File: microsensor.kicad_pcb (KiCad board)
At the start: 2 copper layers, 35 x 47.8 mm, 24 parts, among them J1 ARM SWD, SW1 Control, U1 BMD-360-A-R, U2 RV-3028-C7, U3 HDC2080

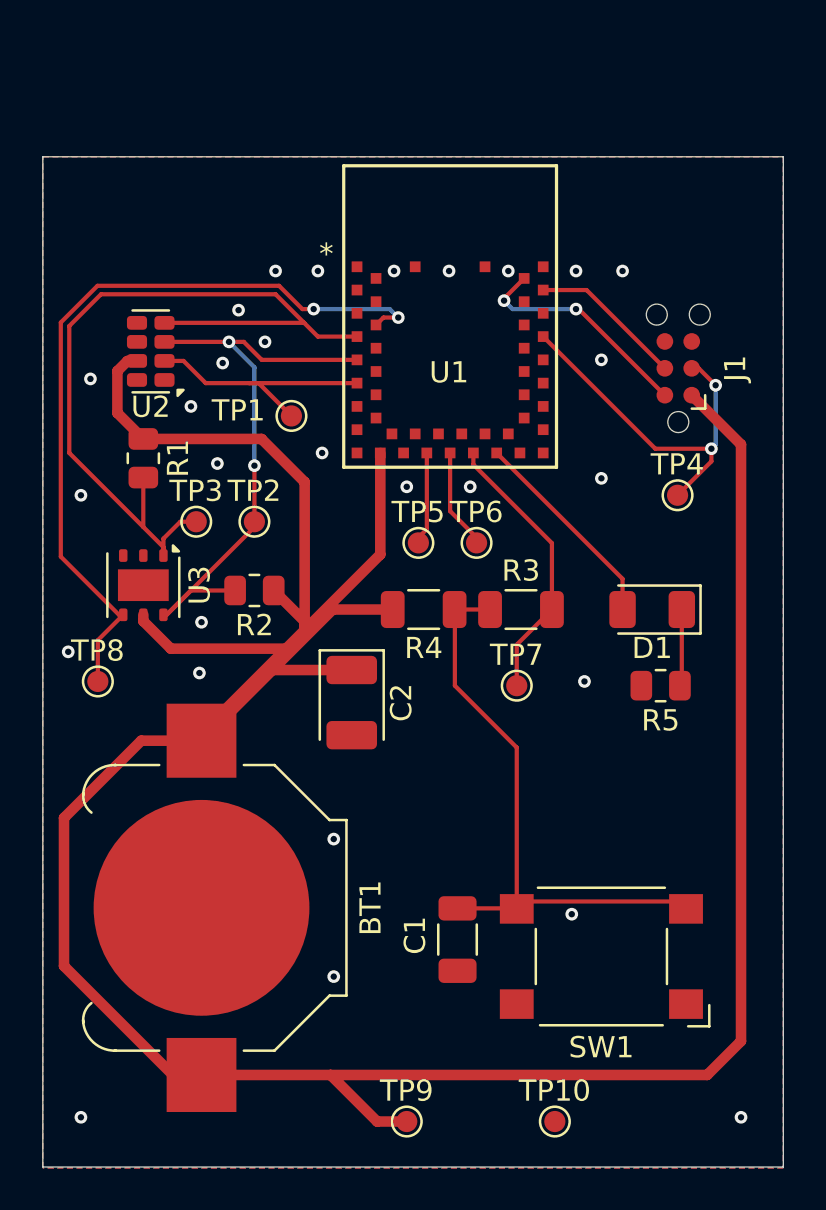
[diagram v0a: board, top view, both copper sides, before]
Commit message: Shrink to 45x35 Unify R sizes to 0805 Rearrange Add dimensions (User layer)
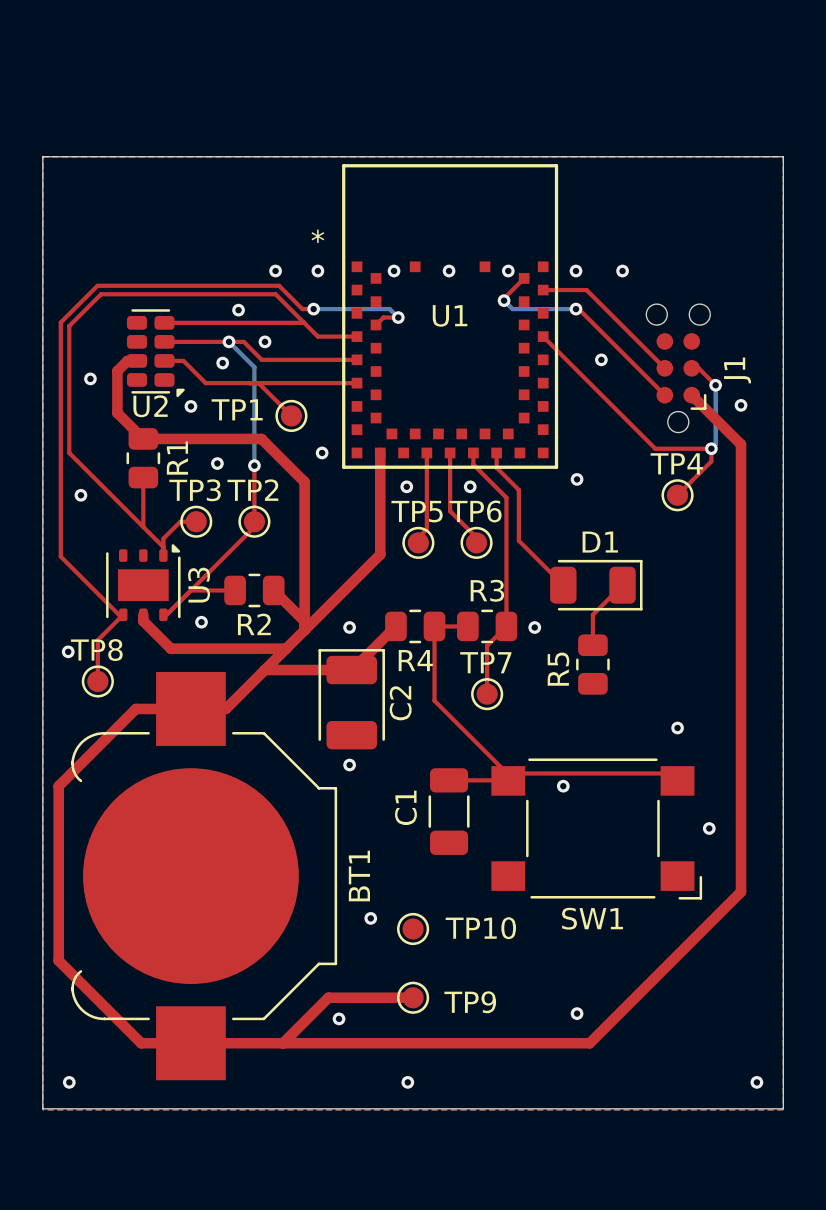
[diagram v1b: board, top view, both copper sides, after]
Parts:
- R3, R4: footprint Resistor_SMD:R_1206_3216Metric -> Resistor_SMD:R_0805_2012Metric
- moved TP10 11.3 mm to (47.5, 66.5)
- moved C1 6.06 mm to (49.2, 61.0)
- moved SW1 6.06 mm to (56.0, 61.8)
- moved TP9 5.86 mm to (47.5, 69.8)
- moved R5 3.35 mm to (56.0, 54.0), turned to -90 degrees
- moved D1 3.03 mm to (56.0, 50.2)
- moved R3 1.79 mm to (51.0, 52.2)
- moved BT1 1.58 mm to (37.0, 64.0)
- moved TP7 1.46 mm to (51.0, 55.4)
- moved R4 0.89 mm to (47.6, 52.2)
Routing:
- net +3V3: track 151.7 -> 138.9 mm
- net Net-(C1-Pad1): track 28.7 -> 22.0 mm
- net Net-(D1-A): track 9.86 -> 7.55 mm
- net SWPUSH: track 13.2 -> 12.4 mm
- net GND: vias 28 -> 34
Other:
- board size 35 x 47.8 mm -> 35 x 45 mm

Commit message: Ver 0.1 finalized and ordered
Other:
- board text added: "BLEsensor v0.1"
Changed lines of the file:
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@@
 				(type "Bottom Silk Screen")
 			)
-			(copper_finish "None")
+			(copper_finish "ENIG")
 			(dielectric_constraints no)
 		)
@@
 			(disableapertmacros no)
 			(usegerberextensions no)
-			(usegerberattributes yes)
+			(usegerberattributes no)
 			(usegerberadvancedattributes yes)
 			(creategerberjobfile yes)
@@
 			(outputformat 1)
 			(mirror no)
-			(drillshape 1)
+			(drillshape 0)
 			(scaleselection 1)
-			(outputdirectory "")
+			(outputdirectory "./CAM")
 		)
 	)
@@
 		(tags "test point SMD pad")
 		(property "Reference" "TP3"
-			(at 0 -1.448 0)
+			(at -0.063609 -1.468763 0)
 			(layer "F.SilkS")
 			(effects
@@
 		(tags "test point SMD pad")
 		(property "Reference" "TP5"
-			(at 0 -1.448 0)
+			(at -0.430648 -1.459986 0)
 			(layer "F.SilkS")
 			(effects
@@
 		(tags "resistor")
 		(property "Reference" "R5"
-			(at 0.227064 1.6 90)
+			(at 0.025 -2.3 180)
 			(layer "F.SilkS")
 			(effects
@@
 		(tags "test point SMD pad")
 		(property "Reference" "TP6"
-			(at 0 -1.448 0)
+			(at 0.257912 -1.459986 0)
 			(layer "F.SilkS")
 			(effects
@@
 		(tags "test point SMD pad")
 		(property "Reference" "TP2"
-			(at 0 -1.448 0)
+			(at 0.38164 -1.459743 0)
 			(layer "F.SilkS")
 			(effects
@@
 			(layer "F.Fab")
 		)
-		(fp_text user "*"
-			(at -6.250001 -3.55 0)
-			(layer "F.SilkS")
-			(effects
-				(font
-					(size 1 1)
-					(thickness 0.15)
-				)
-			)
-		)
 		(fp_text user "${REFERENCE}"
 			(at 0 0 0)
@@
 		(tags "resistor")
 		(property "Reference" "R1"
-			(at 0 -1.65 90)
+			(at 0 1.85 90)
 			(layer "F.SilkS")
 			(effects
@@
 		(tags "test point SMD pad")
 		(property "Reference" "TP1"
-			(at -2.5 -0.25 0)
+			(at -0.825 -1.775 0)
 			(layer "F.SilkS")
 			(effects
@@
 		(layer "Edge.Cuts")
 	)
+	(gr_text "BLEsensor v0.1"
+		(at 63.575 59.5 90)
+		(layer "F.SilkS")
+		(effects
+			(font
+				(size 1 1)
+				(thickness 0.1)
+			)
+			(justify left bottom)
+		)
+	)
 	(dimension

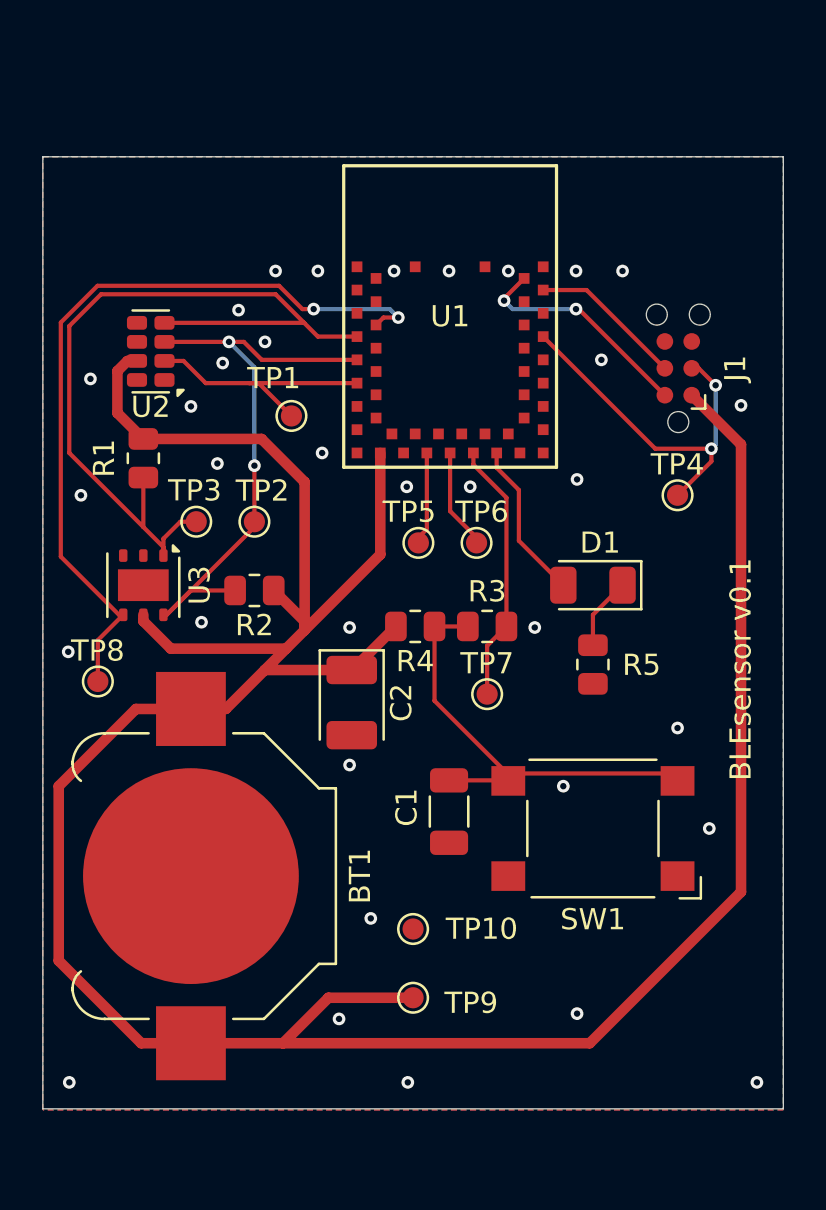
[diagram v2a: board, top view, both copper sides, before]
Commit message: Smaller version 25mmx25mm
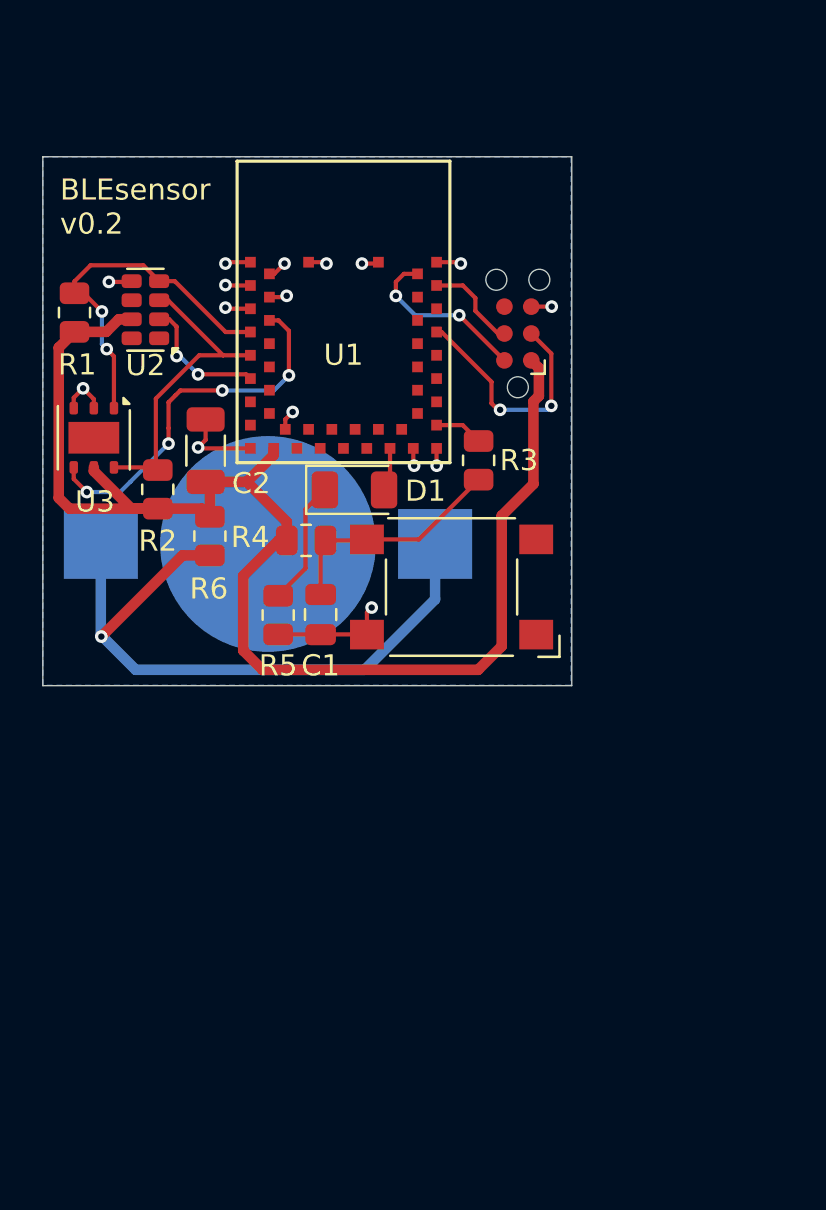
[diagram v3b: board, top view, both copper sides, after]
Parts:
- removed TP1: RTCINT, TestPoint:TestPoint_Pad_D1.0mm
- removed TP10: GND, TestPoint:TestPoint_Pad_D1.0mm
- removed TP2: SCL, TestPoint:TestPoint_Pad_D1.0mm
- removed TP3: SDA, TestPoint:TestPoint_Pad_D1.0mm
- removed TP4: RESET, TestPoint:TestPoint_Pad_D1.0mm
- removed TP5: GPIO 5, TestPoint:TestPoint_Pad_D1.0mm
- removed TP6: GPIO 7, TestPoint:TestPoint_Pad_D1.0mm
- removed TP7: SWPUSH, TestPoint:TestPoint_Pad_D1.0mm
- removed TP8: TEMP_DRDY, TestPoint:TestPoint_Pad_D1.0mm
- removed TP9: 3V3, TestPoint:TestPoint_Pad_D1.0mm
- added R6: 100, Resistor_SMD:R_0805_2012Metric, F.Cu at (37.9, 47.9)
- BT1: moved to B.Cu
- C1: footprint Capacitor_SMD:C_1206_3216Metric -> Capacitor_SMD:C_0805_2012Metric
- C2: footprint Capacitor_Tantalum_SMD:CP_EIA-3528-21_Kemet-B -> Capacitor_SMD:C_1206_3216Metric
- moved BT1 16.1 mm to (40.6, 48.3), turned to 180 degrees
- moved R5 15.1 mm to (41.1, 51.7)
- moved C2 13.8 mm to (37.7, 43.9), turned to 90 degrees
- moved SW1 13.2 mm to (49.3, 50.3)
- moved D1 12.1 mm to (44.7, 45.7), turned to 0 degrees
- moved C1 11.1 mm to (43.1, 51.6)
- moved R3 7.86 mm to (50.6, 44.3), turned to 90 degrees
- moved J1 7.76 mm to (52.5, 38.4)
- moved R1 7.62 mm to (31.5, 37.4), turned to 90 degrees
- moved U3 7.35 mm to (32.4, 43.3)
- moved R2 6.61 mm to (35.4, 45.7), turned to 90 degrees
- moved R4 6.57 mm to (42.4, 48.1)
- moved U1 5.04 mm to (44.2, 37.3)
- moved U2 1.99 mm to (34.8, 37.2)
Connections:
- BT1 pad 1: +3V3 -> /+BAT
- R3 pad 2: SWPUSH -> /SWPUSH
- U1 pad 25: SWPUSH -> unconnected-(U1-P0.09-Pad25)
- U1 pad 31: unconnected-(U1-P0.13-Pad31) -> /SWPUSH
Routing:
- net +3V3: track 138.9 -> 65.6 mm
- net /+BAT: track 0.00 -> 31.5 mm, vias 0 -> 1
- net GND: track 0.00 -> 24.6 mm, vias 34 -> 16
- net SDA: track 39.4 -> 17.0 mm, vias 0 -> 2
- net TEMP_DRDY: track 37.3 -> 17.6 mm, vias 2 -> 4
- net SCL: track 28.2 -> 15.0 mm, vias 2 -> 0
- net SWPUSH: track 12.4 -> 0.00 mm
- net Net-(C1-Pad1): track 22.0 -> 10.7 mm
- net ~{RESET}: track 17.6 -> 11.4 mm
- net RTCINT: track 12.2 -> 6.29 mm, vias 0 -> 2
- net Net-(D1-A): track 7.55 -> 1.68 mm
- net GPIO 7: track 4.52 -> 0.00 mm
- net GPIO 5: track 4.17 -> 0.00 mm
- net SWDCLK: track 7.28 -> 4.50 mm
- net SWDIO: track 10.9 -> 8.24 mm
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- removed copper zone on F.Cu, net GND
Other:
- board size 35 x 45 mm -> 25 x 25 mm
- board text added: "BLEsensor v0.2"
- board text removed: "BLEsensor v0.1"

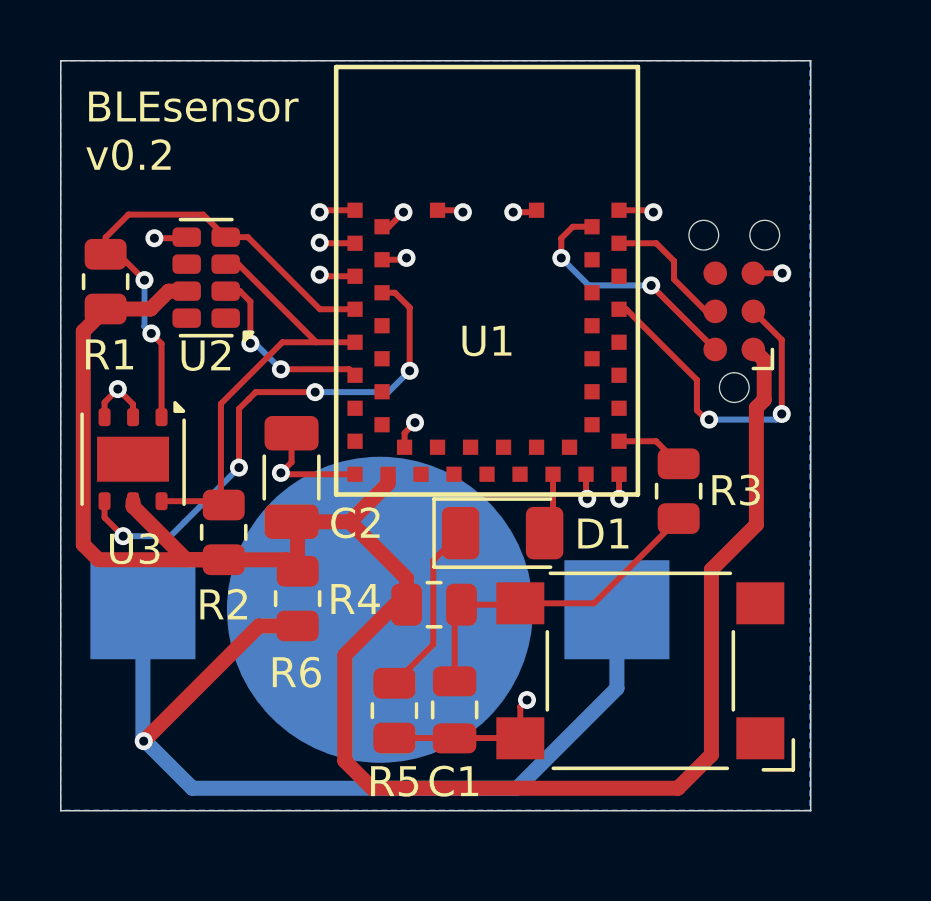
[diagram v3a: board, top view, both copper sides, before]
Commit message: Change battery holder, update layout
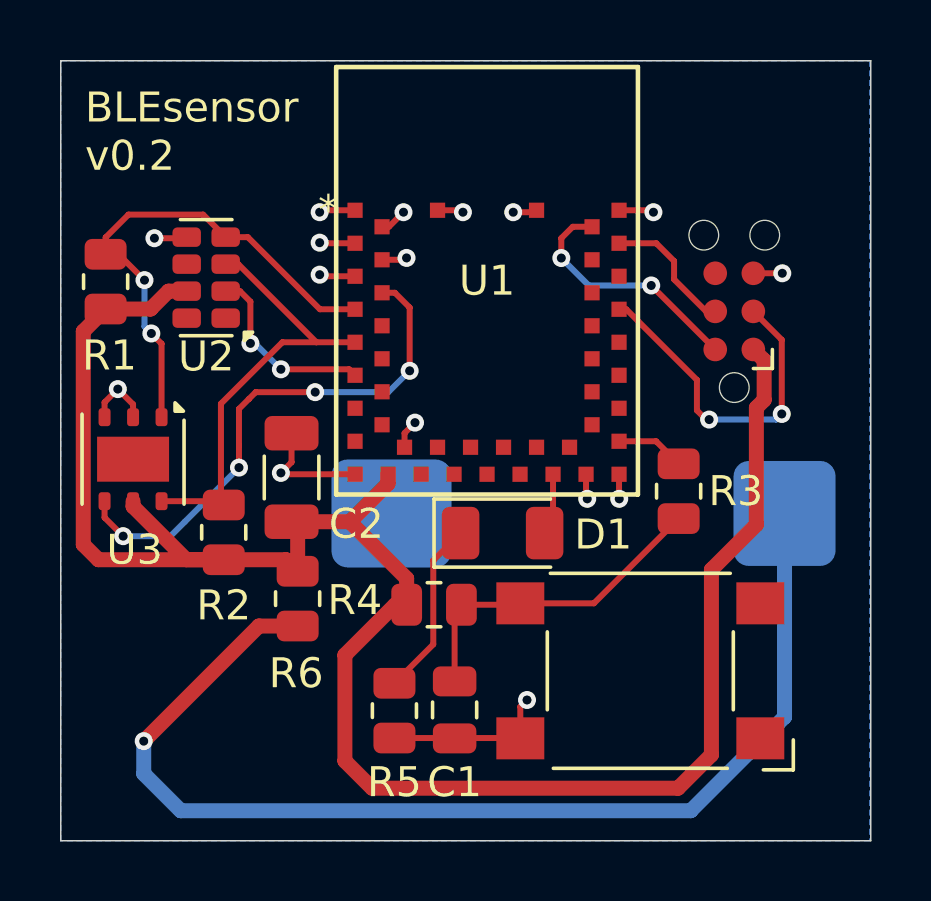
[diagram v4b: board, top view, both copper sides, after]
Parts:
- BT1: footprint Battery:BatteryHolder_Keystone_3000_1x12mm -> footprints:Keystone 110 and 112 for CR20xx
- moved BT1 3.23 mm to (41.0, 45.1)
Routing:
- net /+BAT: track 31.5 -> 37.8 mm
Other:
- board size 25 x 25 mm -> 27 x 26 mm
